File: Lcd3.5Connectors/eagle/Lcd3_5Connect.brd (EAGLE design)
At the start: 11.2 x 49.6 mm, 4 parts

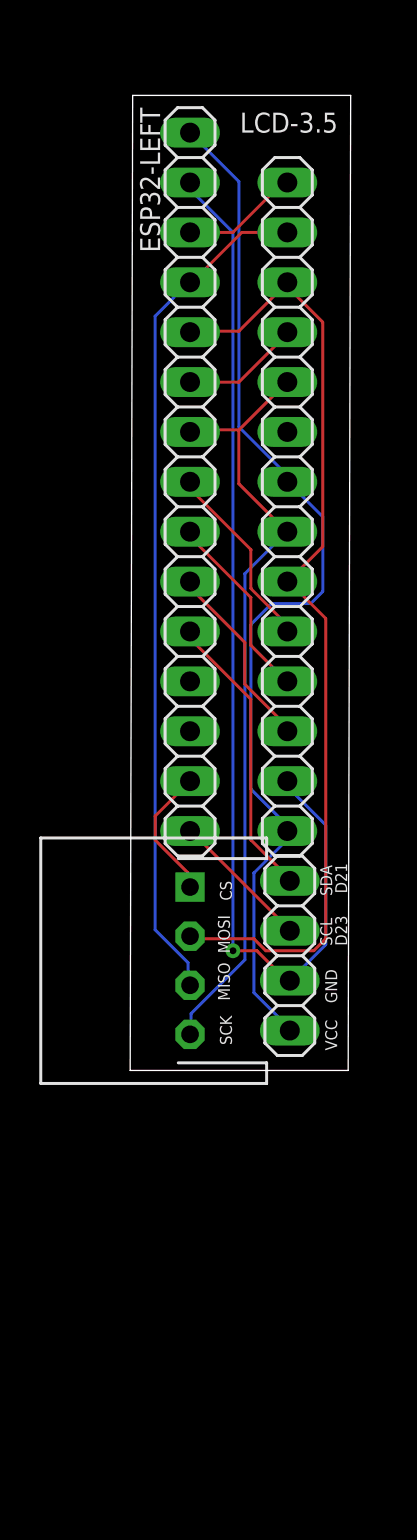
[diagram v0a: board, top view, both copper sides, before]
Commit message: Changed connector orientation
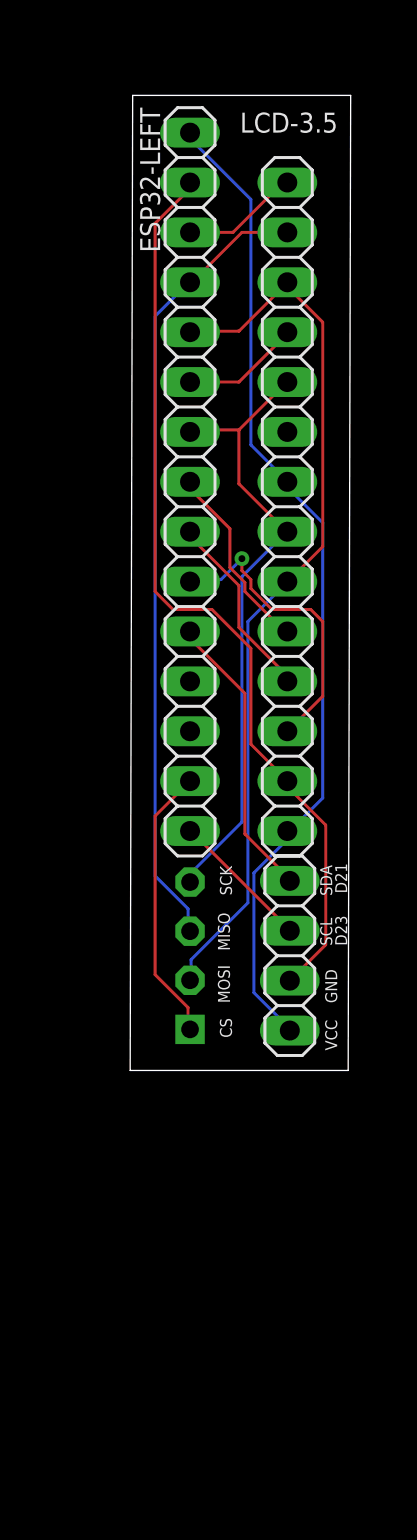
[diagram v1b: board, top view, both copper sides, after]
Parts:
- moved JP1 0.25 mm to (2.54, 27.9), flipped to the bottom, turned to 270 degrees
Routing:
- net GND: track 55.3 -> 46.9 mm, vias 1 -> 0
- net 17: track 39.9 -> 32.2 mm
- net 22: track 6.86 -> 14.1 mm
- net 19: track 9.79 -> 15.6 mm, vias 0 -> 1
- net 4: track 49.3 -> 45.1 mm
- net 2: track 43.3 -> 40.6 mm
- net 3V3: track 53.4 -> 50.8 mm

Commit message: Added 0.50 space
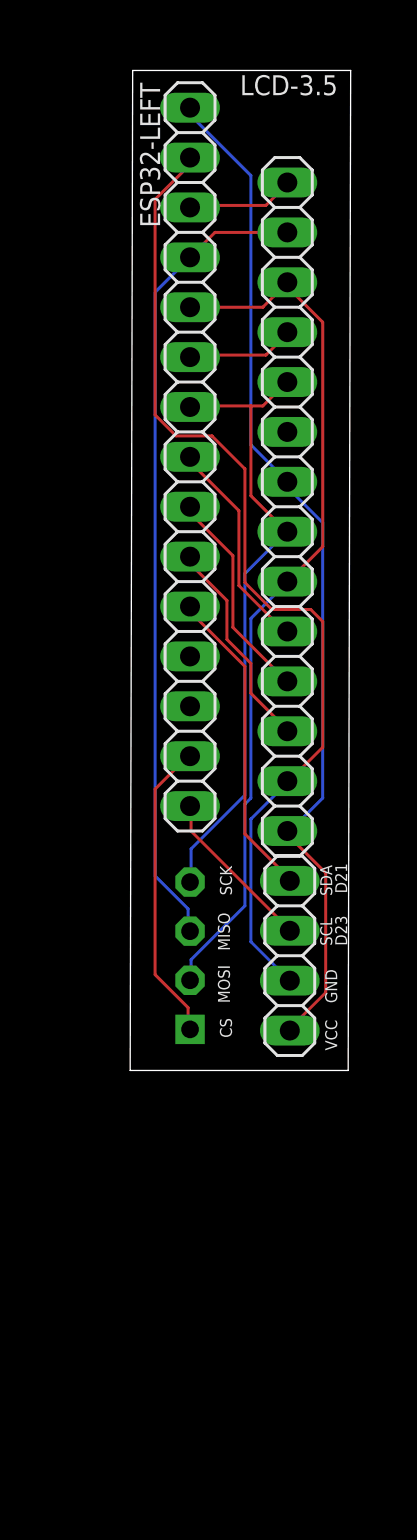
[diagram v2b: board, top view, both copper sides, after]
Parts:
- moved ESP32-LEFT 1.27 mm to (2.54, 53.3)
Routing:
- net 19: track 15.6 -> 10.9 mm, vias 1 -> 0
- net GND: track 46.9 -> 50.8 mm
- net 3V3: track 50.8 -> 52.2 mm
- net 22: track 14.1 -> 15.5 mm
- net 5: track 9.86 -> 11.2 mm
- net 21: track 14.8 -> 16.1 mm
- net 23: track 7.21 -> 8.45 mm
- net 18: track 9.72 -> 11.0 mm
- net 2: track 40.6 -> 41.3 mm
- net 4: track 45.1 -> 44.6 mm
- net 15: track 6.04 -> 5.54 mm
- net 16: track 6.04 -> 5.54 mm
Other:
- board size 11.2 x 49.6 mm -> 11.2 x 50.9 mm

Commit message: Added 3v3 / GND connection
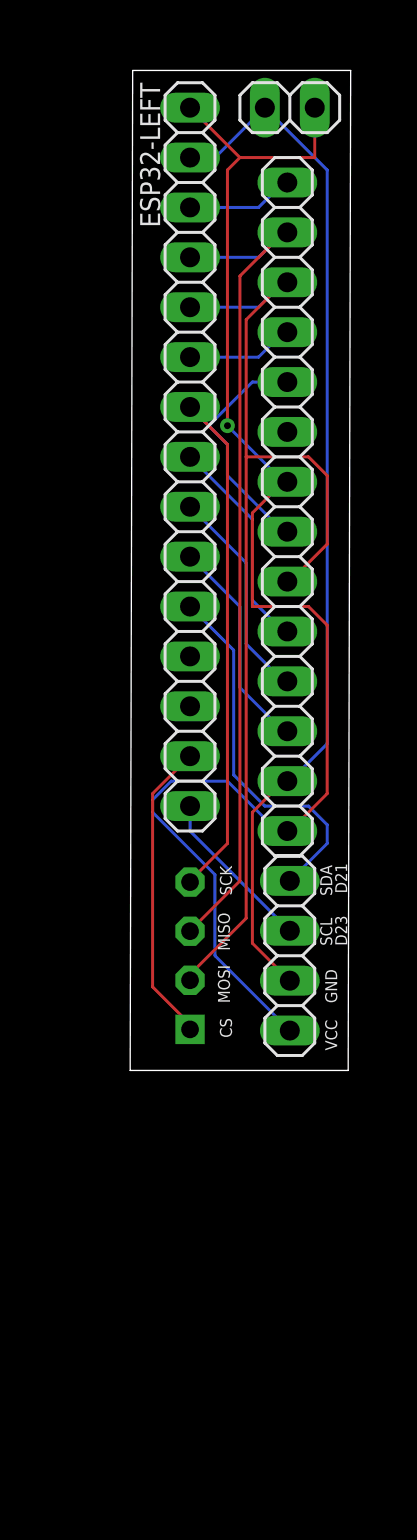
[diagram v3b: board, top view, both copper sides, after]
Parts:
- added JP3: (no value), pinhead:1X02
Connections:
- net 3V3: now also JP3.1
- net GND: now also JP3.2
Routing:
- net 3V3: track 52.2 -> 73.8 mm, vias 0 -> 1
- net 4: track 44.6 -> 54.0 mm
- net 17: track 32.6 -> 39.2 mm
- net 21: track 16.1 -> 19.0 mm
- net GND: track 50.8 -> 53.2 mm
- net 2: track 41.3 -> 43.2 mm
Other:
- board text added: "+"
- board text added: "G"
- board text added: "LCD3.5-V3 T IRQ - 15 T DO - 2 T DIN - 4 T CS - 16 T CLK - 17 LCD MISO - n/c LED - VCC LCD SCK - 17 LCD MOSI - 4 LCD DC/RS - 5 RESET - 18 LCD CS - 19 GND VCC"
- board text removed: "T IRQ - 15 T DO - 2 T DIN - 4 T CS - 16 T CLK - 17 LCD MISO - n/c LED - VCC LCD SCK - 17 LCD MOSI - 4 LCD DC/RS - 5 RESET - 18 LCD CS - 19 GND VCC"

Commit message: Update Lcd3_5Connect.brd
Rotated 3.3v connector
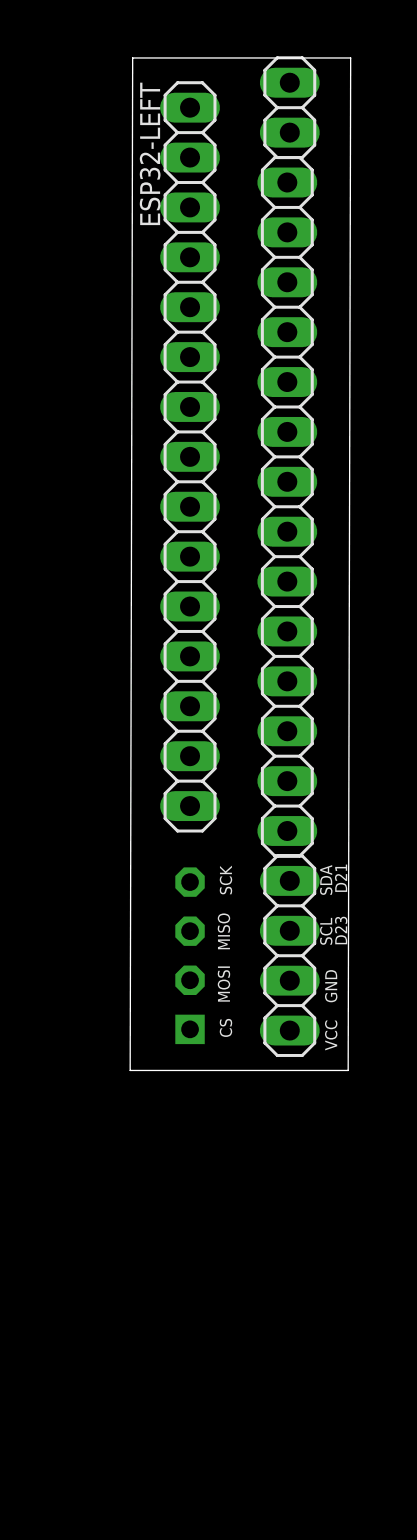
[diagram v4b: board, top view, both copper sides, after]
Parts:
- turned JP3 to 270 degrees
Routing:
- net 3V3: track 73.8 -> 0.00 mm, vias 1 -> 0
- net 4: track 54.0 -> 0.00 mm
- net GND: track 53.2 -> 0.00 mm
- net 2: track 43.2 -> 0.00 mm
- net 17: track 39.2 -> 0.00 mm
- net 21: track 19.0 -> 0.00 mm
- net 22: track 15.5 -> 0.00 mm
- net 18: track 11.1 -> 0.00 mm
- net 19: track 11.1 -> 0.00 mm
- net 5: track 11.1 -> 0.00 mm
- net 23: track 8.45 -> 0.00 mm
- net 16: track 5.48 -> 0.00 mm
- net 15: track 5.48 -> 0.00 mm
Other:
- board size 11.2 x 50.9 mm -> 11.2 x 51.6 mm
- board text added: "G 3v3"
- board text removed: "+"
- board text removed: "G"

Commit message: Added 3v connector space
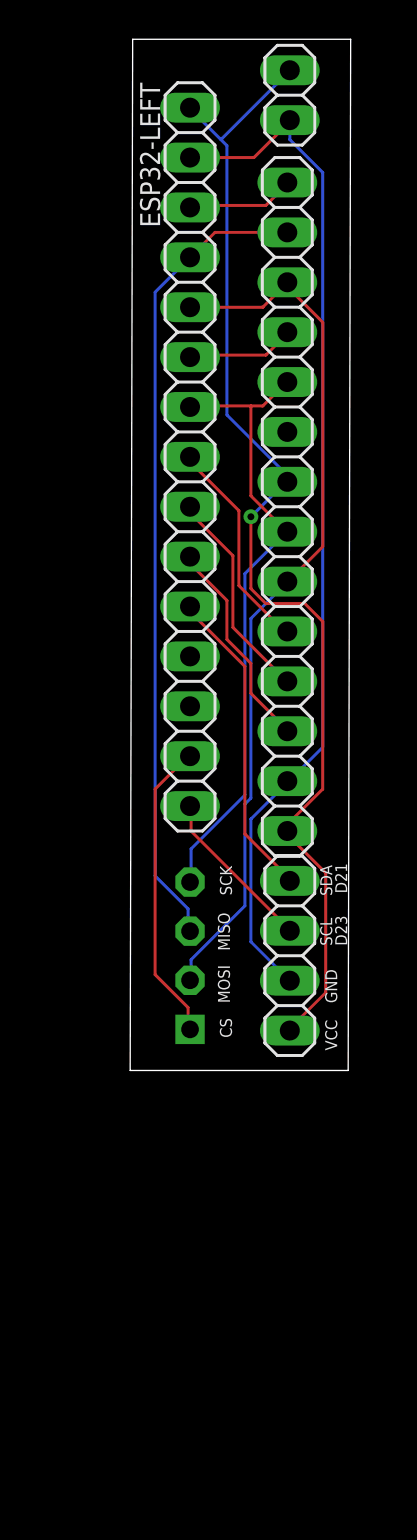
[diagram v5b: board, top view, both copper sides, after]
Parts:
- moved JP3 0.63 mm to (7.62, 71.8)
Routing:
- net 3V3: track 0.00 -> 59.8 mm, vias 0 -> 1
- net GND: track 0.00 -> 52.8 mm
- net 4: track 0.00 -> 44.6 mm
- net 2: track 0.00 -> 41.3 mm
- net 17: track 0.00 -> 32.6 mm
- net 21: track 0.00 -> 16.1 mm
- net 22: track 0.00 -> 15.5 mm
- net 5: track 0.00 -> 11.2 mm
- net 18: track 0.00 -> 11.0 mm
- net 19: track 0.00 -> 10.9 mm
- net 23: track 0.00 -> 8.45 mm
- net 15: track 0.00 -> 5.54 mm
- net 16: track 0.00 -> 5.54 mm
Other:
- board size 11.2 x 51.6 mm -> 11.2 x 52.5 mm

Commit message: Corrected left vs right nomenclature
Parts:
- renumbered ESP32-LEFT to ESP32-RIGHT
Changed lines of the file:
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@@
 <drawing>
 <settings>
-<setting alwaysvectorfont="no"/>
+<setting alwaysvectorfont="yes"/>
 <setting verticaltext="up"/>
 </settings>
@@
 </autorouter>
 <elements>
-<element name="ESP32-LEFT" library="pinhead" library_urn="urn:adsk.eagle:library:325" package="1X15" package3d_urn="urn:adsk.eagle:package:22424/2" value="0" x="2.54" y="53.34" smashed="yes" rot="R270">
+<element name="ESP32-RIGHT" library="pinhead" library_urn="urn:adsk.eagle:library:325" package="1X15" package3d_urn="urn:adsk.eagle:package:22424/2" value="0" x="2.54" y="53.34" smashed="yes" rot="R270">
 <attribute name="NAME" x="0" y="72.39" size="1.016" layer="25" ratio="10" rot="R270"/>
 <attribute name="POPULARITY" value="4" x="-11.43" y="20.32" size="1.778" layer="27" rot="R270" display="off"/>
@@
 <signals>
 <signal name="3V3">
-<contactref element="ESP32-LEFT" pad="1"/>
+<contactref element="ESP32-RIGHT" pad="1"/>
 <contactref element="LCD-3.5" pad="1"/>
 <contactref element="JP2" pad="1"/>
@@
 </signal>
 <signal name="GND">
-<contactref element="ESP32-LEFT" pad="2"/>
+<contactref element="ESP32-RIGHT" pad="2"/>
 <contactref element="LCD-3.5" pad="2"/>
 <contactref element="JP2" pad="2"/>
@@
 </signal>
 <signal name="15">
-<contactref element="ESP32-LEFT" pad="3"/>
+<contactref element="ESP32-RIGHT" pad="3"/>
 <contactref element="LCD-3.5" pad="14"/>
 <wire x1="6.4008" y1="66.1416" x2="2.5908" y2="66.1416" width="0.1524" layer="1"/>
@@
 </signal>
 <signal name="2">
-<contactref element="ESP32-LEFT" pad="4"/>
+<contactref element="ESP32-RIGHT" pad="4"/>
 <contactref element="LCD-3.5" pad="13"/>
 <contactref element="JP1" pad="3"/>
@@
 </signal>
 <signal name="4">
-<contactref element="ESP32-LEFT" pad="5"/>
+<contactref element="ESP32-RIGHT" pad="5"/>
 <contactref element="LCD-3.5" pad="6"/>
 <contactref element="LCD-3.5" pad="12"/>
@@
 </signal>
 <signal name="16">
-<contactref element="ESP32-LEFT" pad="6"/>
+<contactref element="ESP32-RIGHT" pad="6"/>
 <contactref element="LCD-3.5" pad="11"/>
 <wire x1="6.4008" y1="58.5216" x2="2.5908" y2="58.5216" width="0.1524" layer="1"/>
@@
 </signal>
 <signal name="17">
-<contactref element="ESP32-LEFT" pad="7"/>
+<contactref element="ESP32-RIGHT" pad="7"/>
 <contactref element="LCD-3.5" pad="7"/>
 <contactref element="LCD-3.5" pad="10"/>
@@
 </signal>
 <signal name="5">
-<contactref element="ESP32-LEFT" pad="8"/>
+<contactref element="ESP32-RIGHT" pad="8"/>
 <contactref element="LCD-3.5" pad="5"/>
 <wire x1="2.5908" y1="53.0352" x2="2.5908" y2="53.34" width="0.1524" layer="1"/>
@@
 </signal>
 <signal name="18">
-<contactref element="ESP32-LEFT" pad="9"/>
+<contactref element="ESP32-RIGHT" pad="9"/>
 <contactref element="LCD-3.5" pad="4"/>
 <wire x1="2.5908" y1="50.4444" x2="2.5908" y2="50.7492" width="0.1524" layer="1"/>
@@
 </signal>
 <signal name="19">
-<contactref element="ESP32-LEFT" pad="10"/>
+<contactref element="ESP32-RIGHT" pad="10"/>
 <contactref element="LCD-3.5" pad="3"/>
 <wire x1="2.5908" y1="47.8536" x2="2.5908" y2="48.1584" width="0.1524" layer="1"/>
@@
 </signal>
 <signal name="21">
-<contactref element="ESP32-LEFT" pad="11"/>
+<contactref element="ESP32-RIGHT" pad="11"/>
 <contactref element="JP2" pad="4"/>
 <wire x1="2.5908" y1="45.4152" x2="2.5908" y2="45.72" width="0.1524" layer="1"/>
@@
 </signal>
 <signal name="22">
-<contactref element="ESP32-LEFT" pad="14"/>
+<contactref element="ESP32-RIGHT" pad="14"/>
 <contactref element="JP1" pad="1"/>
 <wire x1="2.4384" y1="25.2984" x2="2.4384" y2="24.2316" width="0.1524" layer="1"/>
@@
 </signal>
 <signal name="23">
-<contactref element="ESP32-LEFT" pad="15"/>
+<contactref element="ESP32-RIGHT" pad="15"/>
 <contactref element="JP2" pad="3"/>
 <wire x1="2.5908" y1="34.29" x2="2.5908" y2="35.5092" width="0.1524" layer="1"/>
